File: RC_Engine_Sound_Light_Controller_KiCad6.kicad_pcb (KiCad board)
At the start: 2 copper layers, 87.5 x 40.5 mm, 44 parts, among them J1 RX, J10 RGB, J12 CH1, J13 CH2, J14 CH3, J16 CH4, J17 Brushed Motor output, J2 HeadL, J3 TailL, J4 RoofL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

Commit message: Some minor changes.
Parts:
- added REF**: DiodePolaritySilkscreenSymbol, cf:DiodePolaritySilkscreenSymbol, F.Cu at (85.6, 47.5)
- added REF**: DiodePolaritySilkscreenSymbol, cf:DiodePolaritySilkscreenSymbol, F.Cu at (85.6, 61.1)
- D1, D2: footprint Diode_SMD:D_SMA-SMB_Universal_Handsoldering -> Diode_SMD:D_SMA_Handsoldering
- J1: value RX -> SBUS
- R11: value 570kΩ -> 100kΩ
- R12: value 330kΩ -> 22kΩ
- moved D1 1.27 mm to (85.1, 63.5)
- moved D2 0.89 mm to (85.1, 49.9)
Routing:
- net VCC: track 232.8 -> 231.7 mm
- net Net-(D1-Pad1): track 11.1 -> 10.3 mm
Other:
- board text added: "1:16 Small Crawler PCB v1.2 2022-06-08 by neo2001"
- board text added: "v1.2"
- board text removed: "+5V"
- board text removed: "1:16 Small Crawler PCB v1.1 2022-05-23 by neo2001"
- board text removed: "v1.1"

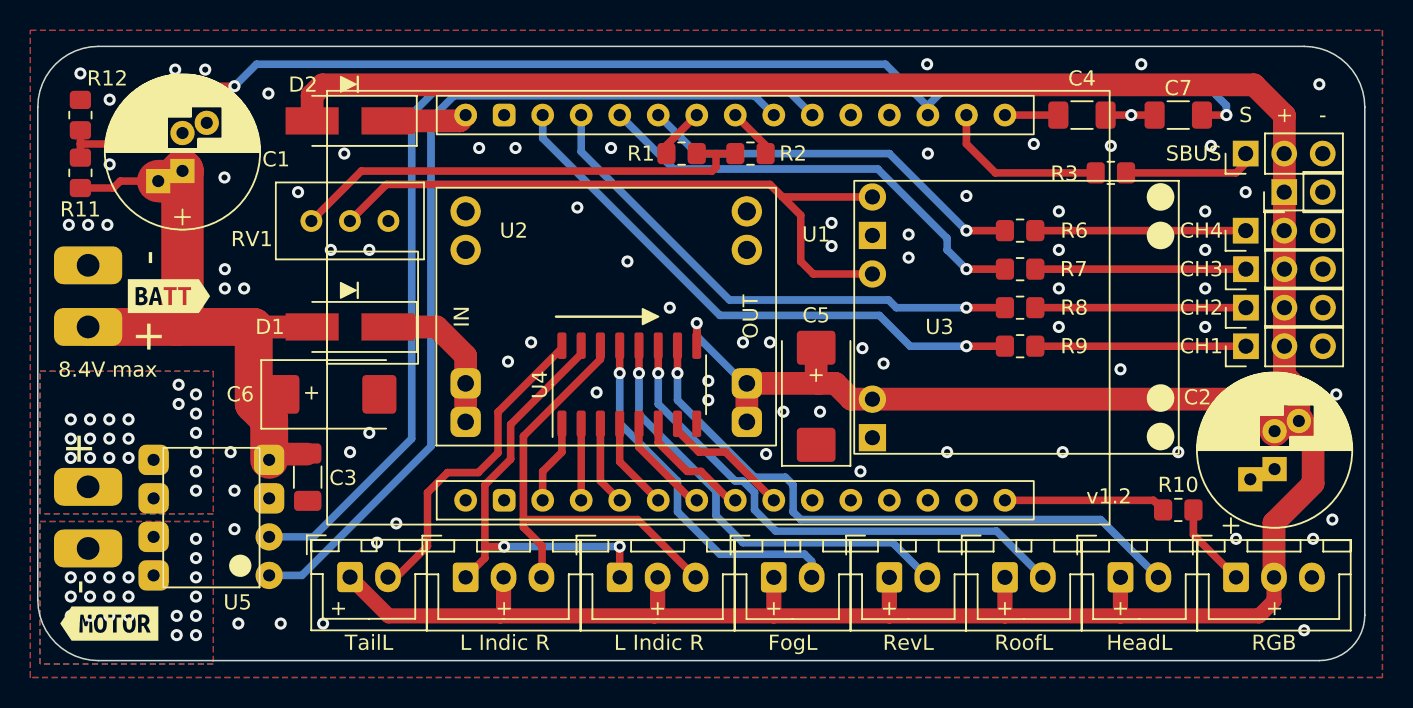
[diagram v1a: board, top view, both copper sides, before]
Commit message: Corrected 5V caps silkscreen polarization.
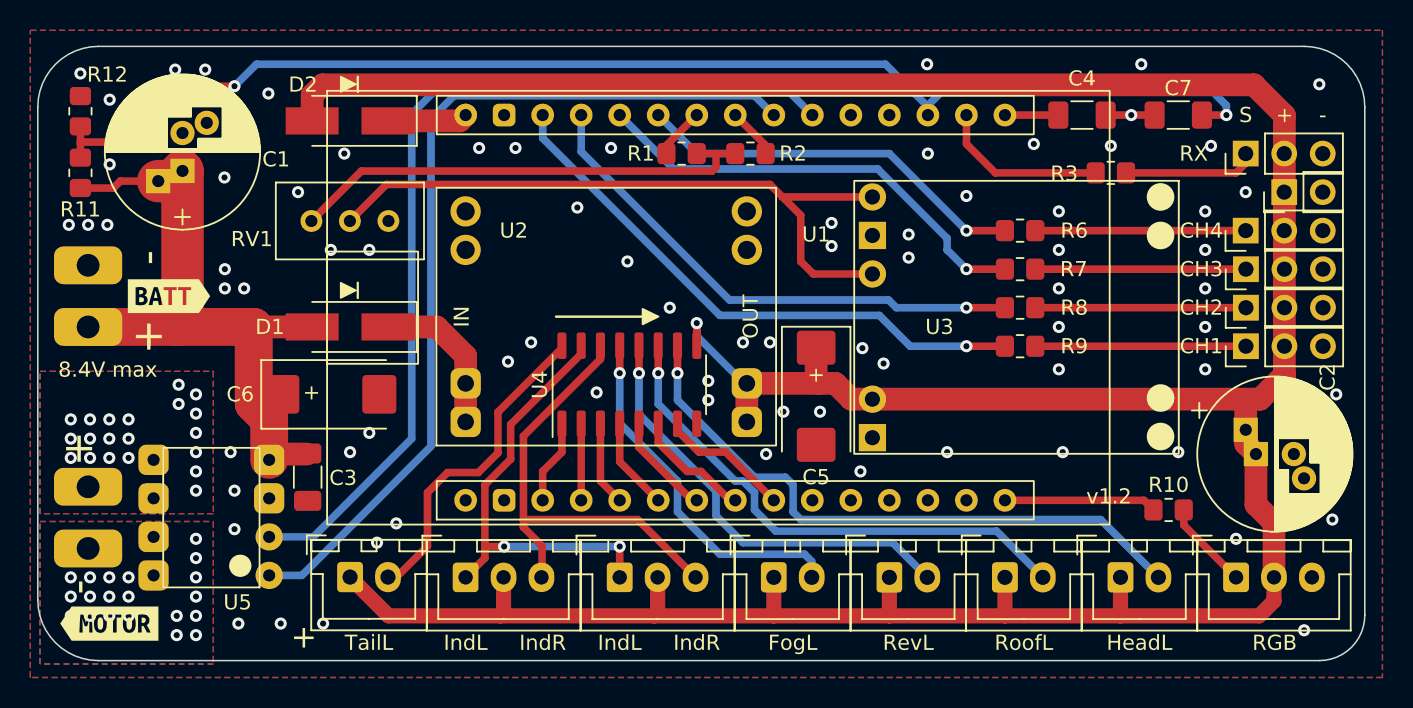
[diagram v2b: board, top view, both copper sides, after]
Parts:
- J1: value SBUS -> RX
- moved C2 1.58 mm to (144.8, 71.9), turned to 0 degrees
- moved R10 0.63 mm to (139.1, 75.6)
- moved R12 0.25 mm to (67.3, 49.3)
- turned C5 to -90 degrees
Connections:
- net Net-(C4-Pad1) renamed /EN_PIN
- net Net-(D1-Pad1) renamed /U2_VIN_PIN
- net Net-(D2-Pad1) renamed /U1_VIN_PIN
- C2 pad 1: -BATT -> VCC
- C2 pad 2: VCC -> -BATT
- C5 pad 1: -BATT -> VCC
- C5 pad 2: VCC -> -BATT
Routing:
- net VCC: track 231.7 -> 224.2 mm
- net D23: track 10.7 -> 10.1 mm
- net -BATT: vias 79 -> 78
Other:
- board text added: "IndL"
- board text added: "IndR"
- board text removed: "L"
- board text removed: "R"

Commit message: Moved input capacitor 1 mm up and away from USB port.
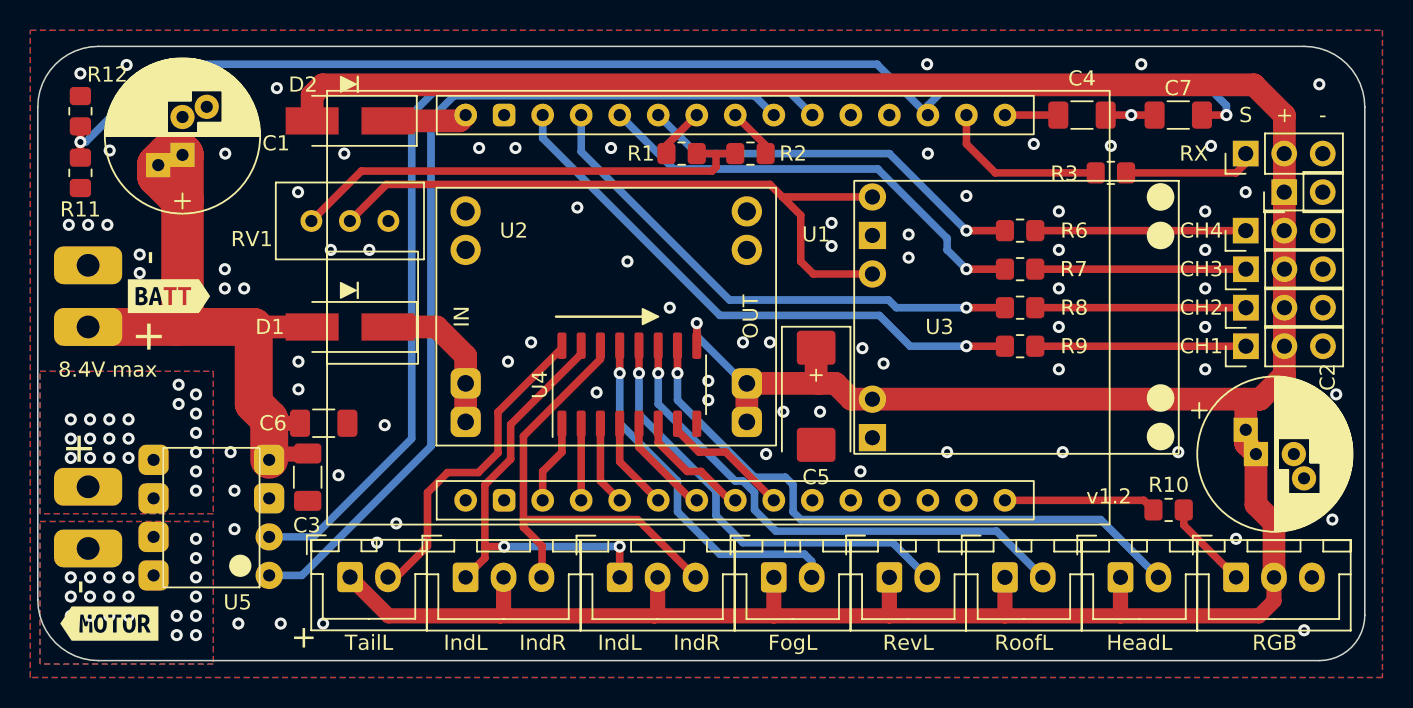
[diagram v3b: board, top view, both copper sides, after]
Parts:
- C1: value 470µF -> 470-1000µF
- C6: value 330µF -> 10µF; footprint Capacitor_Tantalum_SMD:CP_EIA-7343-30_AVX-N_Pad2.25x2.55mm_HandSolder -> Capacitor_SMD:C_1206_3216Metric_Pad1.33x1.80mm_HandSolder
- moved C6 1.96 mm to (83.4, 69.8)
- moved C1 1.06 mm to (74.0, 52.2)
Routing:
- net +BATT: track 43.7 -> 44.6 mm
- net -BATT: vias 78 -> 80

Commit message: Completed voltage divider.
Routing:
- net +BATT: track 44.6 -> 50.3 mm
- net -BATT: vias 80 -> 84
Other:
- board text added: "12.6 V max"
- board text removed: "8.4V max"
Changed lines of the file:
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@@
     (effects (font (size 2 2) (thickness 0.25)))
   )
-  (gr_text "8.4V max" (at 69.1134 66.3194) (layer "F.SilkS")
+  (gr_text "12.6 V\nmax" (at 67.818 67.1068) (layer "F.SilkS")
     (effects (font (size 1 1) (thickness 0.15)))
   )
@@
   (via (at 66.548 56.769) (size 0.8) (drill 0.4) (layers "F.Cu" "B.Cu") (free) (net 10))
   (via (at 118.872 64.897) (size 0.8) (drill 0.4) (layers "F.Cu" "B.Cu") (free) (net 10))
+  (via (at 71.2724 49.8856) (size 0.8) (drill 0.4) (layers "F.Cu" "B.Cu") (free) (net 10))
   (via (at 80.264 47.752) (size 0.8) (drill 0.4) (layers "F.Cu" "B.Cu") (free) (net 10))
   (via (at 83.312 83.058) (size 0.8) (drill 0.4) (layers "F.Cu" "B.Cu") (free) (net 10))
@@
   (via (at 141.478 60.96) (size 0.8) (drill 0.4) (layers "F.Cu" "B.Cu") (free) (net 10))
   (via (at 123.1392 46.1772) (size 0.8) (drill 0.4) (layers "F.Cu" "B.Cu") (free) (net 10))
+  (via (at 70.358 55.2704) (size 0.8) (drill 0.4) (layers "F.Cu" "B.Cu") (free) (net 10))
+  (via (at 71.374 56.2356) (size 0.8) (drill 0.4) (layers "F.Cu" "B.Cu") (free) (net 10))
   (via (at 77.724 83.058) (size 0.8) (drill 0.4) (layers "F.Cu" "B.Cu") (free) (net 10))
   (via (at 131.826 55.88) (size 0.8) (drill 0.4) (layers "F.Cu" "B.Cu") (free) (net 10))
@@
   (via (at 116.078 69.088) (size 0.8) (drill 0.4) (layers "F.Cu" "B.Cu") (free) (net 10))
   (via (at 110.998 64.516) (size 0.8) (drill 0.4) (layers "F.Cu" "B.Cu") (free) (net 10))
+  (via (at 76.8604 55.9816) (size 0.8) (drill 0.4) (layers "F.Cu" "B.Cu") (free) (net 10))
   (via (at 108.712 68.326) (size 0.8) (drill 0.4) (layers "F.Cu" "B.Cu") (free) (net 10))
   (via (at 71.2216 59.944) (size 0.8) (drill 0.4) (layers "F.Cu" "B.Cu") (free) (net 10))
@@
   (via (at 95.504 65.786) (size 0.8) (drill 0.4) (layers "F.Cu" "B.Cu") (free) (net 10))
   (via (at 81.6864 65.786) (size 0.8) (drill 0.4) (layers "F.Cu" "B.Cu") (free) (net 10))
-  (via (at 69.2404 51.8668) (size 0.8) (drill 0.4) (layers "F.Cu" "B.Cu") (free) (net 10))
+  (via (at 69.342 51.816) (size 0.8) (drill 0.4) (layers "F.Cu" "B.Cu") (free) (net 10))
   (segment (start 134.255 53.34) (end 127.635 53.34) (width 0.5) (layer "F.Cu") (net 13))
   (segment (start 125.73 51.435) (end 125.73 49.53) (width 0.5) (layer "F.Cu") (net 13))
@@
   (segment (start 78.74 63.5) (end 82.59 63.5) (width 1.5) (layer "F.Cu") (net 42))
   (segment (start 73.66 63.5) (end 78.74 63.5) (width 2.5) (layer "F.Cu") (net 42))
+  (segment (start 69.0024 54.34) (end 70.514463 52.827937) (width 0.7) (layer "F.Cu") (net 42))
   (segment (start 81.788 69.85) (end 80.033949 69.85) (width 1) (layer "F.Cu") (net 42))
   (segment (start 74.041 52.157) (end 73.111937 52.157) (width 2.8) (layer "F.Cu") (net 42))
@@
   (segment (start 74.041 55.118) (end 74.041 63.119) (width 2.8) (layer "F.Cu") (net 42))
   (segment (start 72.441 52.827937) (end 72.441 53.518) (width 2.8) (layer "F.Cu") (net 42))
+  (segment (start 70.514463 52.827937) (end 72.441 52.827937) (width 0.7) (layer "F.Cu") (net 42))
   (segment (start 78.74 63.5) (end 78.74 68.556051) (width 2.5) (layer "F.Cu") (net 42))
   (segment (start 67.818 63.5) (end 73.66 63.5) (width 2.5) (layer "F.Cu") (net 42))
@@
   (segment (start 74.041 52.157) (end 74.041 55.118) (width 2.8) (layer "F.Cu") (net 42))
   (segment (start 80.137 71.882) (end 82.2575 71.882) (width 1) (layer "F.Cu") (net 42))
+  (segment (start 67.31 54.34) (end 69.0024 54.34) (width 0.7) (layer "F.Cu") (net 42))
   (segment (start 74.041 63.119) (end 73.66 63.5) (width 2) (layer "F.Cu") (net 42))
   (via (at 70.485 72.136) (size 0.8) (drill 0.4) (layers "F.Cu" "B.Cu") (free) (net 43))

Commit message: Minor changes.
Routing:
- net /MOTOR_FO: vias 20 -> 19
- net /MOTOR_BO: vias 20 -> 19
- net -BATT: vias 84 -> 89

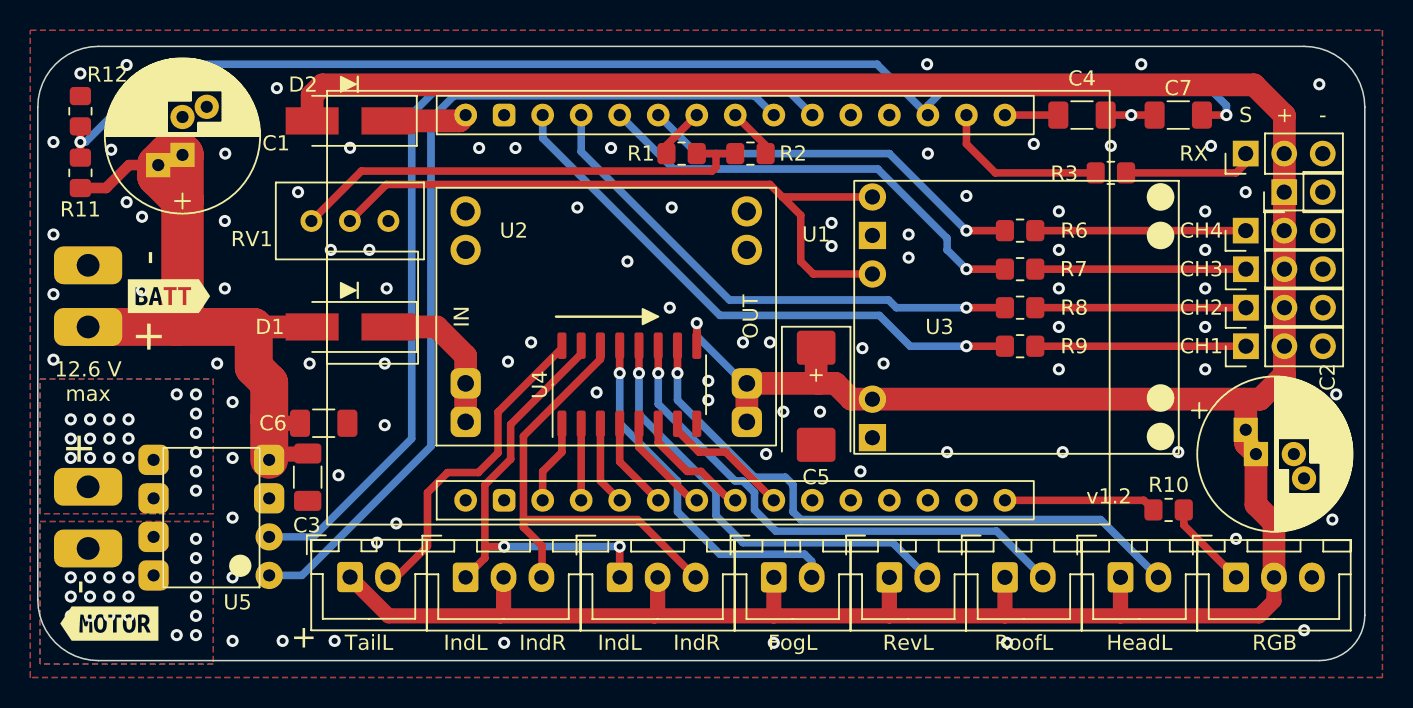
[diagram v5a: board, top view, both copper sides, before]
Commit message: Added solder jumper between VCC and VDD.
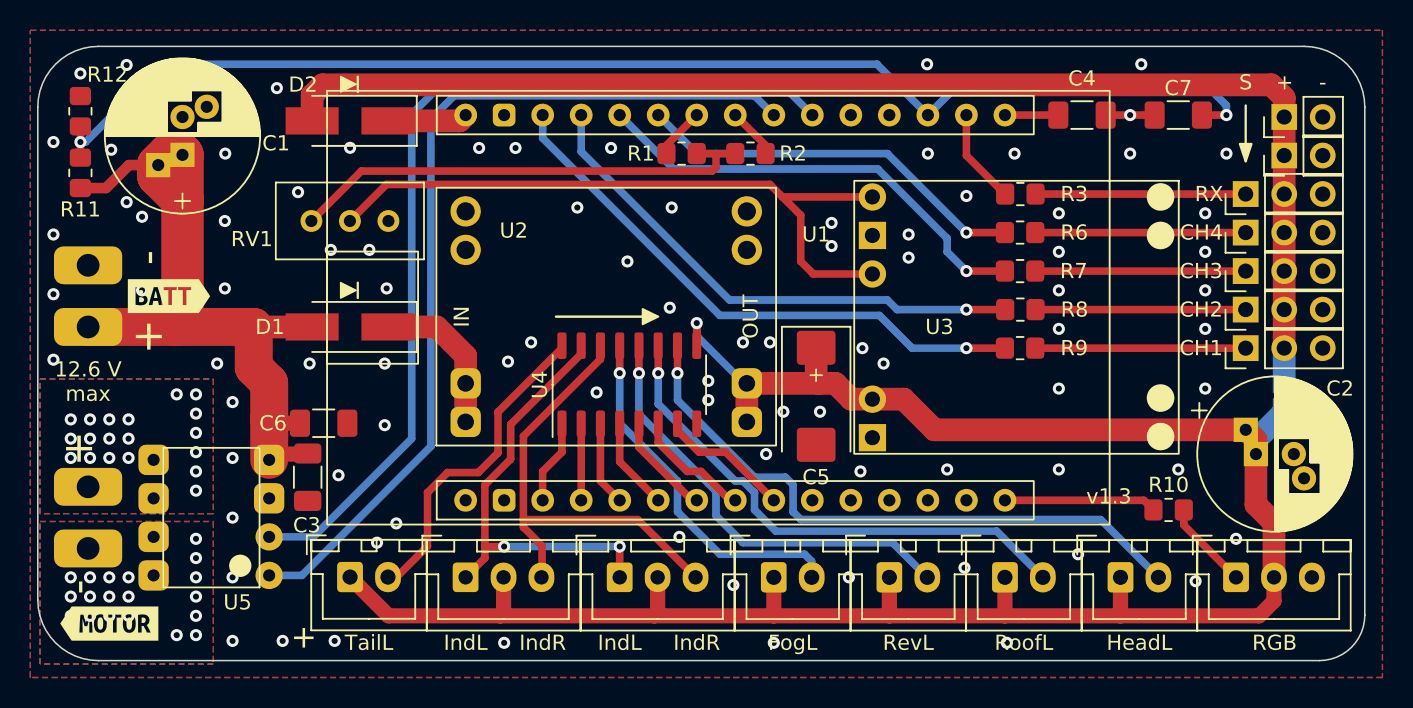
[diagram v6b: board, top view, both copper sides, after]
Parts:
- added JP1: VCC to VDD, Jumper:SolderJumper-2_P1.3mm_Open_TrianglePad1.0x1.5mm, B.Cu at (146.7, 67.7)
- added REF**: PinHeader_1x02_P2.54mm_Vertical, Connector_PinHeader_2.54mm:PinHeader_1x02_P2.54mm_Vertical, F.Cu at (146.7, 52.2)
- moved R3 6.13 mm to (129.3, 54.7)
- moved REF** 4.95 mm to (146.7, 49.7)
- moved J1 2.67 mm to (144.1, 54.7)
- moved R8 0.13 mm to (129.3, 62.4)
- moved J12 0.13 mm to (144.1, 64.9)
- moved J13 0.13 mm to (144.1, 62.4)
- moved J14 0.13 mm to (144.1, 59.8)
- moved R9 0.13 mm to (129.3, 64.9)
- moved J16 0.13 mm to (144.1, 57.3)
- moved R6 0.13 mm to (129.3, 57.3)
- moved R7 0.13 mm to (129.3, 59.8)
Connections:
- D2 pad 2: VCC -> VDD
- J1 pad 2: VCC -> VDD
- J12 pad 2: VCC -> VDD
- J13 pad 2: VCC -> VDD
- J14 pad 2: VCC -> VDD
- J16 pad 2: VCC -> VDD
- REF** pad 1: VCC -> VDD
- REF** pad 2: GND -> -BATT
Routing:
- net VCC: track 224.2 -> 138.4 mm
- net VDD: track 0.00 -> 84.2 mm
- net /RX: track 8.79 -> 13.9 mm
- net D36: track 11.2 -> 6.26 mm
- net -BATT: vias 89 -> 90
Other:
- board text added: "1:16 Small Crawler PCB v1.3 July 2022, by neo2001"
- board text added: "VCC"
- board text added: "VDD"
- board text added: "v1.3"
- board text removed: "1:16 Small Crawler PCB v1.2 2022-06-08 by neo2001"
- board text removed: "v1.2"

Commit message: Fixed wrong headlight pin (moved from D18 to D3).
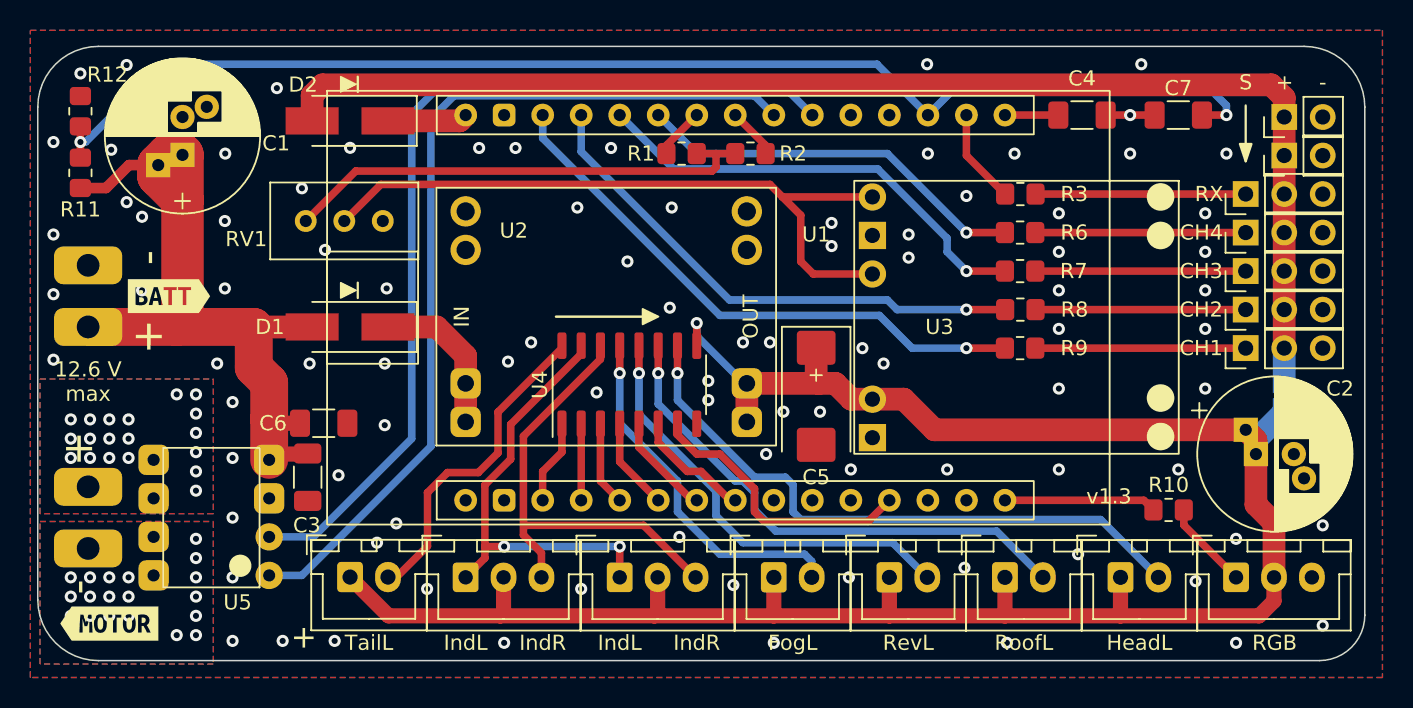
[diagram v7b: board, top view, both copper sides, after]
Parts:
- moved RV1 0.37 mm to (82.2, 56.5)
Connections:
- U1 pad 12: unconnected-(U1-Pad12) -> D3
- U1 pad 9: D18 -> unconnected-(U1-Pad9)
- U4 pad 7: D18 -> D3
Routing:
- net D3: track 0.00 -> 18.5 mm
- net D18: track 8.25 -> 0.00 mm
- net -BATT: vias 90 -> 94
